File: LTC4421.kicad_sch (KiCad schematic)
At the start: 38 parts, among them U2 LTC4421CG-PBF

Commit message: Library fixes and sch changes
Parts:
- removed CMOSFET1, CMOSFET2: 10u, ECE319K:C_Axial_200mil, symbol ECE319K:C
- removed D3, D4: GREEN, ECE319K:LED_D5.0mm, symbol ECE319K:LED
- removed D5, D6: RED, ECE319K:LED_D5.0mm, symbol ECE319K:LED
- removed D7, D8: BLUE, ECE319K:LED_D5.0mm, symbol ECE319K:LED
- removed R17, R18: 5K, Resistor_SMD:R_0805_2012Metric, symbol Device:R
- removed RETRY_PD1, SHDN_PU1, VAL2_PU1, VAL_PU1: 10k, Resistor_SMD:R_0805_2012Metric, symbol Device:R
- removed SHDN_Switch1, SHDN_Switch2: UP, ECE319K:SW_PUSH_6mm, symbol ECE319K:SW_Push
- added C3, C5: 0.1u, ECE319K:C_Axial_200mil, symbol ECE319K:C
- added C4: 10u, ECE319K:C_Axial_200mil, symbol ECE319K:C
- added D3, D4, D5, D6, D7, D8: LED, symbol Device:LED
- added JP1: DIS1 Jumper, symbol Jumper:Jumper_3_Open
- added JP2: DIS2 Jumper, symbol Jumper:Jumper_3_Open
- added JP3: RETRY Jumper, symbol Jumper:Jumper_3_Open
- added R19, R20, R21, R22, R23, R24, R25, R26, R27, R28: 100K, Resistor_SMD:R_0805_2012Metric, symbol Device:R
- added TP1, TP2, TP3, TP4: TestPoint, symbol Connector:TestPoint
- added U3, U4, U5: 74LVC2G07GV,125, symbol PowerBoardLib:74LVC2G07GV,125
- R11, R12, R13, R14, R15, R16: value 5K -> 100K
- U2: symbol LTC4221:LTC4421CG-PBF -> PowerBoardLib:LTC4421CG-PBF
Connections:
- net CH1: now also R21.2, U5.3 (2A)
- net CH2: now also R22.2, U4.3 (2A)
- net DISABLE1: now also JP1.2 (C), R19.2; no longer CINTV_CC1.1, U2.16 (CASIN), U2.17 (INTVCC), U2.25 (*DISABLE2)
- net FAULT1: now also R25.2, U3.1 (1A)
- net FAULT2: now also R26.2, U3.3 (2A)
- net GND: now also C3.2, C4.2, C5.2, JP1.1 (A), JP2.1 (A), JP3.1 (A), U3.2 (GND), U4.2 (GND), U5.2 (GND)
- net OUT: now also C3.1, C4.1, C5.1, D5.2 (A), D6.2 (A), D7.2 (A), D8.2 (A)
- net RETRY: now also JP3.2 (C), R27.2; no longer R12.2
- net SHDN: now also R28.2; no longer R11.2
- net V2: now also D3.2 (A), D4.2 (A); no longer R11.1, R12.1, R13.1, R14.1, R15.1, R16.1
- net VALID1: now also R23.2, U5.1 (1A)
- net VALID2: now also R24.2, U4.1 (1A)
- net at R15.2: now also U5.6 (1Y)
- net Non-Crit Drive: now reaches R14.2
- net Non-Crit Drive: now also U4.4 (2Y)
- net at R16.2: now also U5.4 (2Y)
- net at R13.2: now also U4.6 (1Y)
- new net: D5.1 (K), R13.1
- new net: D4.1 (K), R12.1
- new net: R12.2, U3.4 (2Y)
- new net: D8.1 (K), R16.1
- new net: D7.1 (K), R15.1
- new net: D6.1 (K), R14.1
- new net: D3.1 (K), R11.1
- new net: R11.2, U3.6 (1Y)
- new net DISABLE2: JP2.2 (C), R20.2, U2.25 (*DISABLE2)
- new net INTVCC: R19.1, R20.1, R21.1, R22.1, R23.1, R24.1, R25.1, R26.1, R27.1, R28.1, U3.5 (VCC), U4.5 (VCC), U5.5 (VCC)
- new net INTV_CC: CINTV_CC1.1, U2.16 (CASIN), U2.17 (INTVCC)
- no-connect marks 1 -> 4
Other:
- note added: "Decoupling Capacitors"
- note added: "Disable"
- note added: "Enable"
- note added: "Jumpers"
- note added: "LEDs"
- note added: "No Retry"
- note added: "Pullups"
- note added: "Using buffer"
- note removed: "DC-DC Convertor MOSFETs"
- note removed: "FAULT LEDs"
- note removed: "For the future, we should include a microcontroller so we can precisely control DISABLE, RETRY, and SHDN"
- note removed: "MOSFET Capacitors"
- note removed: "Output LEDs"
- note removed: "Retry Circuitry"
- note removed: "SHDN Circuitry"
- note removed: "Shutdown"
- note removed: "Supplemental Battery MOSFETs"
- note removed: "VALID LEDs"

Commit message: Sch changes
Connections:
- net VALID2: now also R13.2, U4.6 (1Y)
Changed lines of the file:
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@@
 		(color 0 0 0 0)
 	)
+	(junction
+		(at 156.21 93.98)
+		(diameter 0)
+		(color 0 0 0 0)
+	)
 	(no_connect
 		(at 31.75 71.12)
@@
 	(wire
 		(pts
-			(xy 69.85 60.96) (xy 80.01 60.96)
-		)
-		(stroke
-			(width 0)
-			(type default)
-		)
-	)
-	(wire
-		(pts
 			(xy 130.81 62.23) (xy 139.7 62.23)
 		)
@@
 	(wire
 		(pts
+			(xy 69.85 60.96) (xy 77.47 60.96)
+		)
+		(stroke
+			(width 0)
+			(type default)
+		)
+	)
+	(wire
+		(pts
 			(xy 130.81 66.04) (xy 139.7 66.04)
 		)
@@
 	(wire
 		(pts
+			(xy 156.21 93.98) (xy 158.75 93.98)
+		)
+		(stroke
+			(width 0)
+			(type default)
+		)
+	)
+	(wire
+		(pts
 			(xy 110.49 184.15) (xy 118.11 184.15)
 		)
@@
 	(wire
 		(pts
-			(xy 154.94 93.98) (xy 158.75 93.98)
+			(xy 154.94 93.98) (xy 156.21 93.98)
 		)
 		(stroke
@@
 	(wire
 		(pts
+			(xy 157.48 100.33) (xy 156.21 100.33)
+		)
+		(stroke
+			(width 0)
+			(type default)
+		)
+	)
+	(wire
+		(pts
 			(xy 158.75 83.82) (xy 158.75 85.09)
 		)
@@
 	(wire
 		(pts
+			(xy 156.21 100.33) (xy 156.21 93.98)
+		)
+		(stroke
+			(width 0)
+			(type default)
+		)
+	)
+	(wire
+		(pts
 			(xy 77.47 55.88) (xy 69.85 55.88)
 		)
@@
 	(wire
 		(pts
-			(xy 154.94 99.06) (xy 156.21 99.06)
+			(xy 154.94 102.87) (xy 157.48 102.87)
 		)
 		(stroke
@@
 	(wire
 		(pts
-			(xy 154.94 96.52) (xy 154.94 99.06)
+			(xy 154.94 96.52) (xy 154.94 102.87)
 		)
 		(stroke
@@
 	(wire
 		(pts
-			(xy 21.59 60.96) (xy 31.75 60.96)
+			(xy 24.13 48.26) (xy 31.75 48.26)
 		)
 		(stroke
@@
 	(wire
 		(pts
-			(xy 24.13 48.26) (xy 31.75 48.26)
+			(xy 69.85 43.18) (xy 77.47 43.18)
 		)
 		(stroke
@@
 	(wire
 		(pts
-			(xy 69.85 43.18) (xy 77.47 43.18)
+			(xy 93.98 184.15) (xy 101.6 184.15)
 		)
 		(stroke
@@
 	(wire
 		(pts
-			(xy 93.98 184.15) (xy 101.6 184.15)
+			(xy 24.13 33.02) (xy 31.75 33.02)
 		)
 		(stroke
@@
 	(wire
 		(pts
-			(xy 24.13 33.02) (xy 31.75 33.02)
+			(xy 24.13 60.96) (xy 31.75 60.96)
 		)
 		(stroke
@@
 		)
 	)
-	(hierarchical_label "VALID1"
-		(shape output)
-		(at 21.59 60.96 180)
-		(fields_autoplaced yes)
-		(effects
-			(font
-				(size 1.27 1.27)
-			)
-			(justify right)
-		)
-	)
 	(hierarchical_label "GATE1"
 		(shape output)
@@
 	(hierarchical_label "VALID2"
 		(shape output)
-		(at 80.01 60.96 0)
+		(at 157.48 100.33 0)
 		(fields_autoplaced yes)
 		(effects
@@
 	(hierarchical_label "Non-Crit Drive"
 		(shape output)
-		(at 156.21 99.06 0)
+		(at 157.48 102.87 0)
 		(fields_autoplaced yes)
 		(effects

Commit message: changes to sch
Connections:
- net VALID2: no longer R13.2, U4.6 (1Y)
- new net: R13.2, U4.6 (1Y)
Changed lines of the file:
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@@
 		(color 0 0 0 0)
 	)
-	(junction
-		(at 156.21 93.98)
-		(diameter 0)
-		(color 0 0 0 0)
-	)
 	(no_connect
 		(at 31.75 71.12)
@@
 	(wire
 		(pts
-			(xy 156.21 93.98) (xy 158.75 93.98)
-		)
-		(stroke
-			(width 0)
-			(type default)
-		)
-	)
-	(wire
-		(pts
 			(xy 110.49 184.15) (xy 118.11 184.15)
 		)
@@
 	(wire
 		(pts
-			(xy 154.94 93.98) (xy 156.21 93.98)
+			(xy 154.94 93.98) (xy 158.75 93.98)
 		)
 		(stroke
@@
 	(wire
 		(pts
-			(xy 157.48 100.33) (xy 156.21 100.33)
-		)
-		(stroke
-			(width 0)
-			(type default)
-		)
-	)
-	(wire
-		(pts
 			(xy 158.75 83.82) (xy 158.75 85.09)
 		)
@@
 	(wire
 		(pts
-			(xy 156.21 100.33) (xy 156.21 93.98)
-		)
-		(stroke
-			(width 0)
-			(type default)
-		)
-	)
-	(wire
-		(pts
 			(xy 77.47 55.88) (xy 69.85 55.88)
 		)
@@
 		)
 	)
-	(hierarchical_label "VALID2"
-		(shape output)
-		(at 157.48 100.33 0)
-		(fields_autoplaced yes)
-		(effects
-			(font
-				(size 1.27 1.27)
-			)
-			(justify left)
-		)
-	)

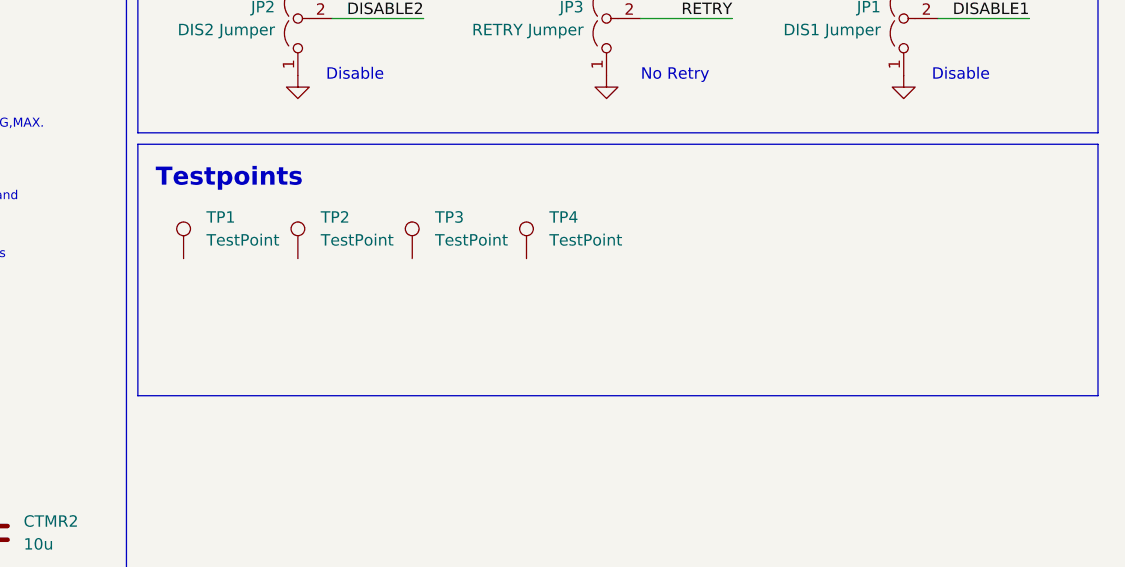
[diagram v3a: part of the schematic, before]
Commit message: assigned footprints
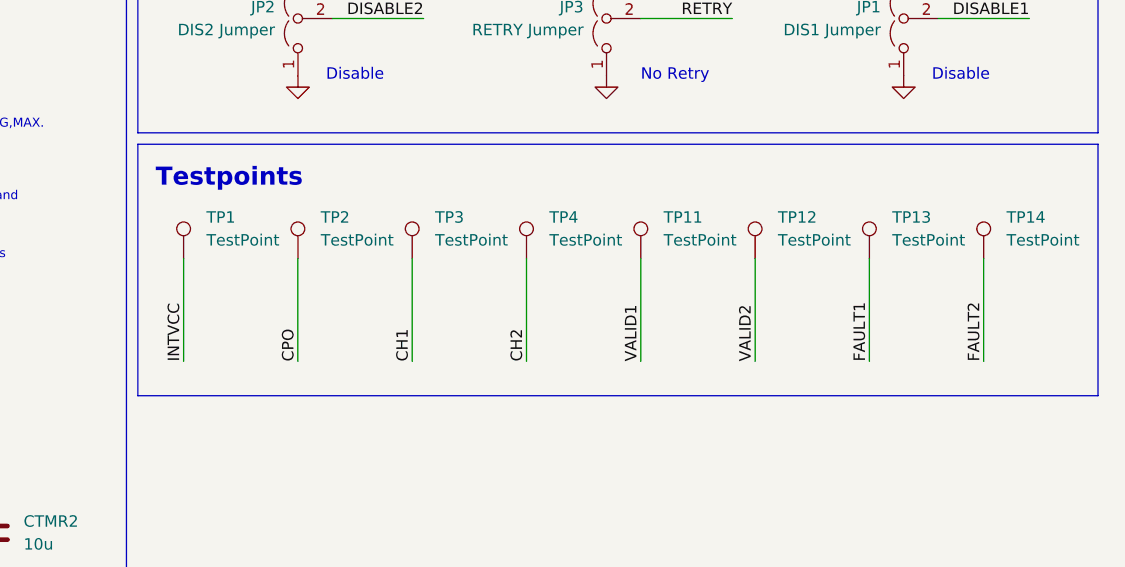
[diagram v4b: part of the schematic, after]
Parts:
- added TP11, TP12, TP13, TP14: TestPoint, UTSVT_Special:TestPoint_HEX_3mmID, symbol Connector:TestPoint
- C3, C4, C5: footprint ECE319K:C_Axial_200mil -> Capacitor_SMD:C_0805_2012Metric
- CCPO1, CINTV_CC1, CQUAL1, CTMR1, CTMR2: footprint ECE319K:C_Axial_200mil -> (none)
- COUT1: footprint Capacitor_SMD:C_0805_2012Metric -> (none)
- D3, D4, D5, D6, D7, D8: footprint (none) -> LED_SMD:LED_0805_2012Metric
- JP1, JP2, JP3: footprint (none) -> Connector_PinHeader_1.00mm:PinHeader_1x03_P1.00mm_Vertical
- RSENSE1: footprint Resistor_SMD:R_0805_2012Metric -> (none)
- TP1, TP2, TP3, TP4: footprint (none) -> UTSVT_Special:TestPoint_HEX_3mmID
- U2: footprint LTC4421:G_05-08-1640_ADI -> PowerBoardLib:G_05-08-1640_ADI
- U3, U4, U5: footprint (none) -> Package_TO_SOT_SMD:ROHM_SOT-457_ClockwisePinNumbering
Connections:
- net CH1: now also TP3.1
- net CH2: now also TP4.1
- net CPO: now also TP2.1
- net FAULT1: now also TP13.1
- net FAULT2: now also TP14.1
- net INTVCC: now also TP1.1
- net VALID1: now also TP11.1
- net VALID2: now also TP12.1

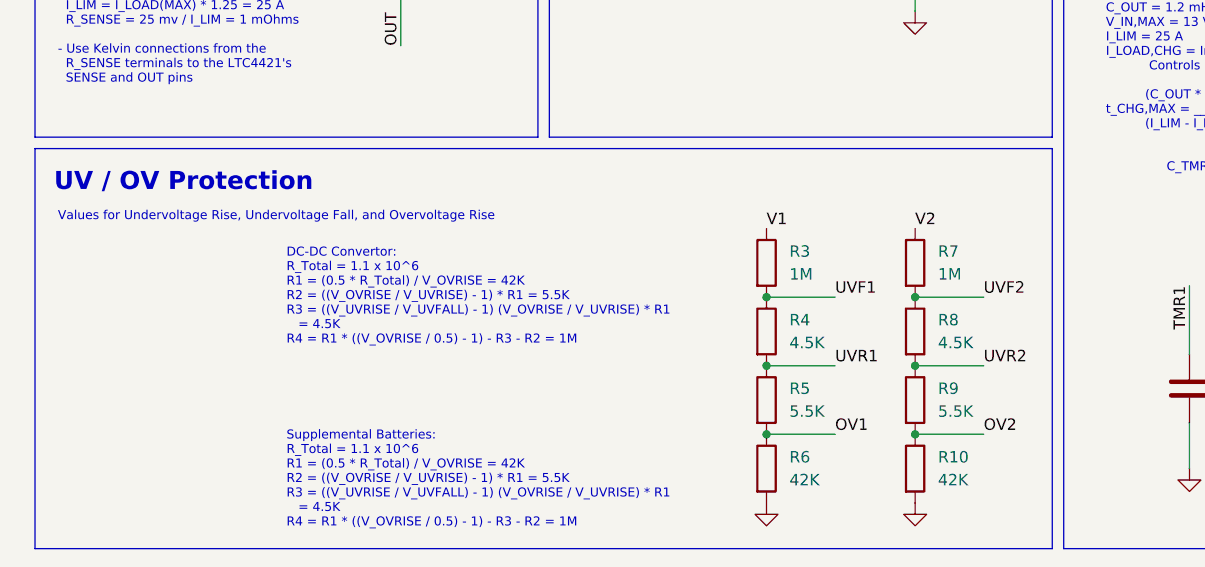
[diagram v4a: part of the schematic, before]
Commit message: Adjusted resistor divider values and specified more components in the BOM
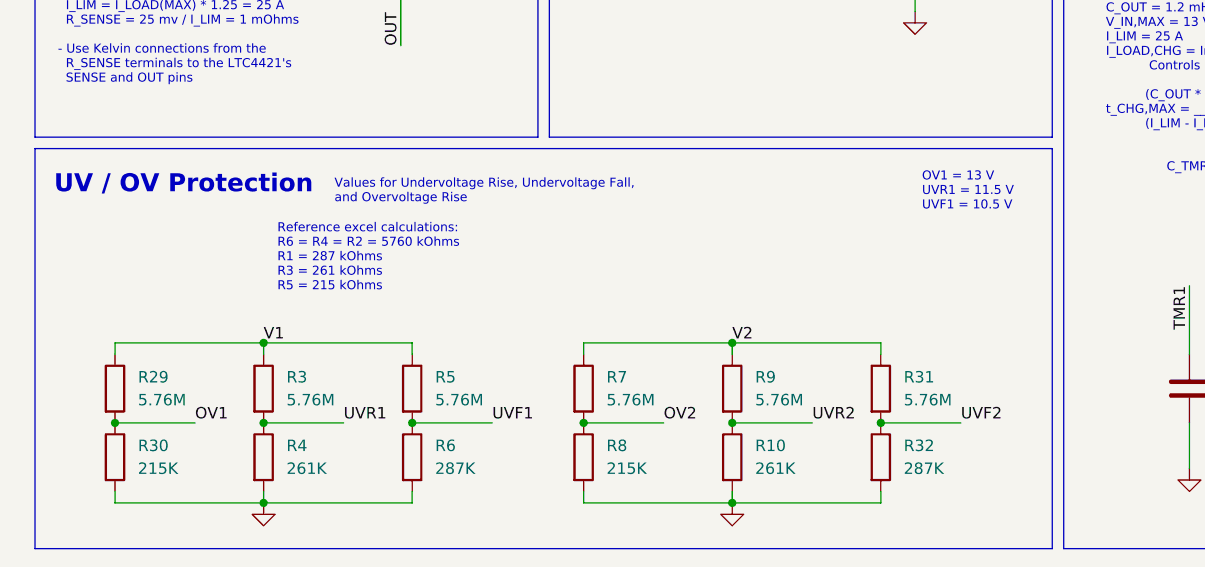
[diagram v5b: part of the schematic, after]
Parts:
- added R29, R31: 5.76M, Resistor_SMD:R_0805_2012Metric, symbol Device:R
- added R30: 215K, Resistor_SMD:R_0805_2012Metric, symbol Device:R
- added R32: 287K, Resistor_SMD:R_0805_2012Metric, symbol Device:R
- C3, C5: MFG PN (none) -> C0805C104M5RACTU
- C4, CTMR1, CTMR2: MFG PN (none) -> TMK212BBJ106MGHT
- CCPO1, CINTV_CC1: footprint (none) -> Capacitor_SMD:C_0805_2012Metric; MFG PN (none) -> C0805C105K5PACTU
- COUT1: MFG PN (none) -> ESW128M016AH5AA
- D3, D4, D5, D6, D7, D8: MFG PN (none) -> APTD2012LCGCK
- R10: value 42K -> 261K; MFG PN (none) -> RC0805FR-07261KL
- R11, R12, R13, R14, R15, R16, R19, R20, R21, R22, R23, R24, R25, R26, R27, R28: MFG PN (none) -> CRCW0805100KFKEAC
- R3, R7: value 1M -> 5.76M; MFG PN (none) -> RC0805FR-075M76L
- R4: value 4.5K -> 261K; MFG PN (none) -> RC0805FR-07261KL
- R5, R9: value 5.5K -> 5.76M; MFG PN (none) -> RC0805FR-075M76L
- R6: value 42K -> 287K; MFG PN (none) -> CRCW0805287KFKEA
- R8: value 4.5K -> 215K; MFG PN (none) -> RC0805FR-07215KL
- U2: MFG PN (none) -> LTC4421CG-PBF
- U3, U4, U5: MFG PN (none) -> 74LVC2G07GV,125
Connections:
- net GND: now also R4.2, R8.2, R30.2, R32.2
- net OV1: now also R29.2, R30.1; no longer R5.2, R6.1
- net OV2: now also R7.2, R8.1; no longer R10.1, R9.2
- net UVF1: now also R5.2, R6.1; no longer R3.2, R4.1
- net UVF2: now also R31.2, R32.1; no longer R7.2, R8.1
- net UVR1: now also R3.2, R4.1; no longer R4.2, R5.1
- net UVR2: now also R10.1, R9.2; no longer R8.2, R9.1
- net V1: now also R5.1, R29.1
- net V2: now also R9.1, R31.1
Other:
- note added: "OV1 = 13 V UVR1 = 11.5 V UVF1 = 10.5 V"
- note added: "Reference excel calculations: R6 = R4 = R2 = 5760 kOhms R1 = 287 kOhms R3 = 261 kOhms R5 = 215 kOhms"
- note removed: "DC-DC Convertor: R_Total = 1.1 x 10^6 R1 = (0.5 * R_Total) / V_OVRISE = 42K R2 = ((V_OVRISE / V_UVRISE) - 1) * R1 = 5.5K R3 = ((V_UVRISE / V_UVFALL) - 1) (V_OVRISE / V_UVRISE) * R1 = 4.5K R4 = R1 * ((V_OVRISE / 0.5) - 1) - R3 - R2 = 1M"
- note removed: "Supplemental Batteries: R_Total = 1.1 x 10^6 R1 = (0.5 * R_Total) / V_OVRISE = 42K R2 = ((V_OVRISE / V_UVRISE) - 1) * R1 = 5.5K R3 = ((V_UVRISE / V_UVFALL) - 1) (V_OVRISE / V_UVRISE) * R1 = 4.5K R4 = R1 * ((V_OVRISE / 0.5) - 1) - R3 - R2 = 1M"
- moved on the sheet: R5, R6

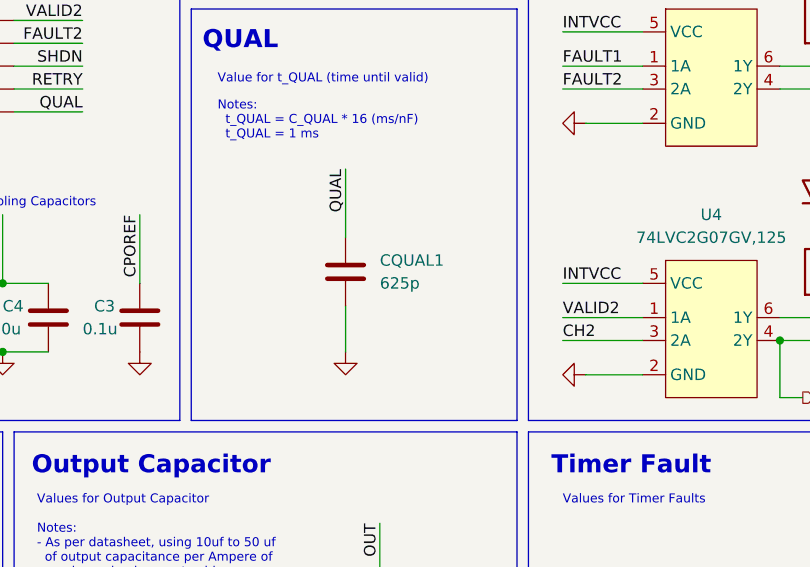
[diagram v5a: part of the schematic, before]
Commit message: Completed BOM for the most part
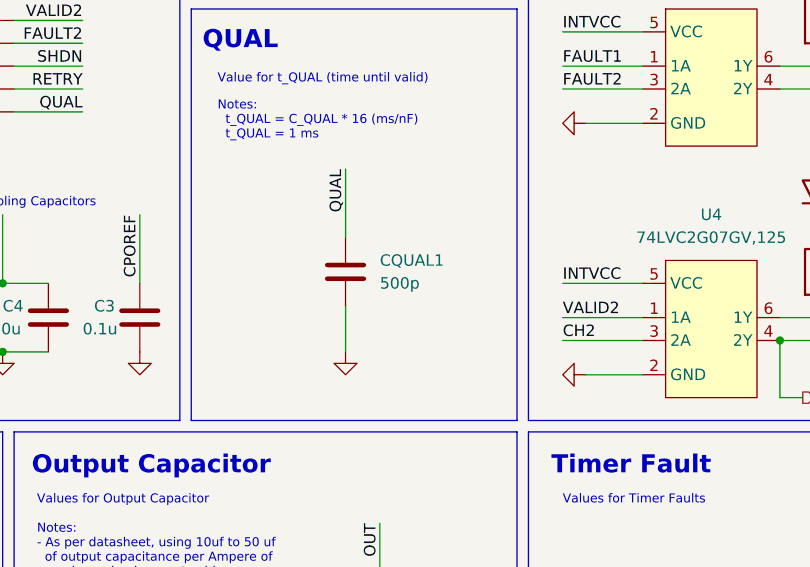
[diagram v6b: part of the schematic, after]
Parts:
- COUT1: footprint (none) -> PowerBoardLib:EEUFS1C122LB
- CQUAL1: value 625p -> 500p; footprint (none) -> Capacitor_SMD:C_0603_1608Metric; MFG PN (none) -> CC0603KRX7R9BB501
- RSENSE1: footprint (none) -> Resistor_SMD:R_0603_1608Metric; MFG PN (none) -> PA0603FRP7W0R001L
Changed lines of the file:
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@@
 			)
 		)
-		(property "Value" "625p"
+		(property "Value" "500p"
 			(at 110.49 90.1699 0)
 			(effects
@@
 			)
 		)
-		(property "Footprint" ""
+		(property "Footprint" "Capacitor_SMD:C_0603_1608Metric"
 			(at 107.6452 92.71 0)
 			(effects
@@
 			)
 		)
-		(property "Datasheet" "~"
+		(property "Datasheet" "https://www.yageo.com/upload/media/product/productsearch/datasheet/mlcc/UPY-GPHC_X7R_6.3V-to-250V_24.pdf"
 			(at 106.68 88.9 0)
 			(effects
@@
 			)
 		)
-		(property "MFG PN" ""
+		(property "MFG PN" "CC0603KRX7R9BB501"
 			(at 106.68 88.9 0)
 			(effects
@@
 			)
 		)
-		(property "Footprint" ""
+		(property "Footprint" "PowerBoardLib:EEUFS1C122LB"
 			(at 110.49 128.27 0)
 			(effects
@@
 			)
 		)
-		(property "Footprint" ""
+		(property "Footprint" "Resistor_SMD:R_0603_1608Metric"
 			(at 51.562 128.27 90)
 			(effects
@@
 			)
 		)
-		(property "Datasheet" "~"
+		(property "Datasheet" "https://mm.digikey.com/Volume0/opasdata/d220001/medias/docus/6352/YAGEO%20Datasheet_PA0603_1mR_L_0_RoHS_P_TCR.pdf"
 			(at 53.34 128.27 0)
 			(effects
@@
 			)
 		)
-		(property "MFG PN" ""
+		(property "MFG PN" "PA0603FRP7W0R001L"
 			(at 53.34 128.27 0)
 			(effects
